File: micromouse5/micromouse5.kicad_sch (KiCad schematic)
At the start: 69 parts, among them J1 Conn_01x06_Pin, J2 Conn_01x06_Pin, J3 JST 2, J4 JST 1, J5 Conn_01x04_Pin, Q1 IR Receiver, Q2 IR Receiver, Q3 IR Receiver, Q4 IR Receiver, SW1 Button, SW2 EG1218, U1 HBridge, U2 Voltage Regulator, U3 MOSFET, U4 MOSFET, U5 MOSFET, U6 MOSFET, U7 STM32F205RGTx

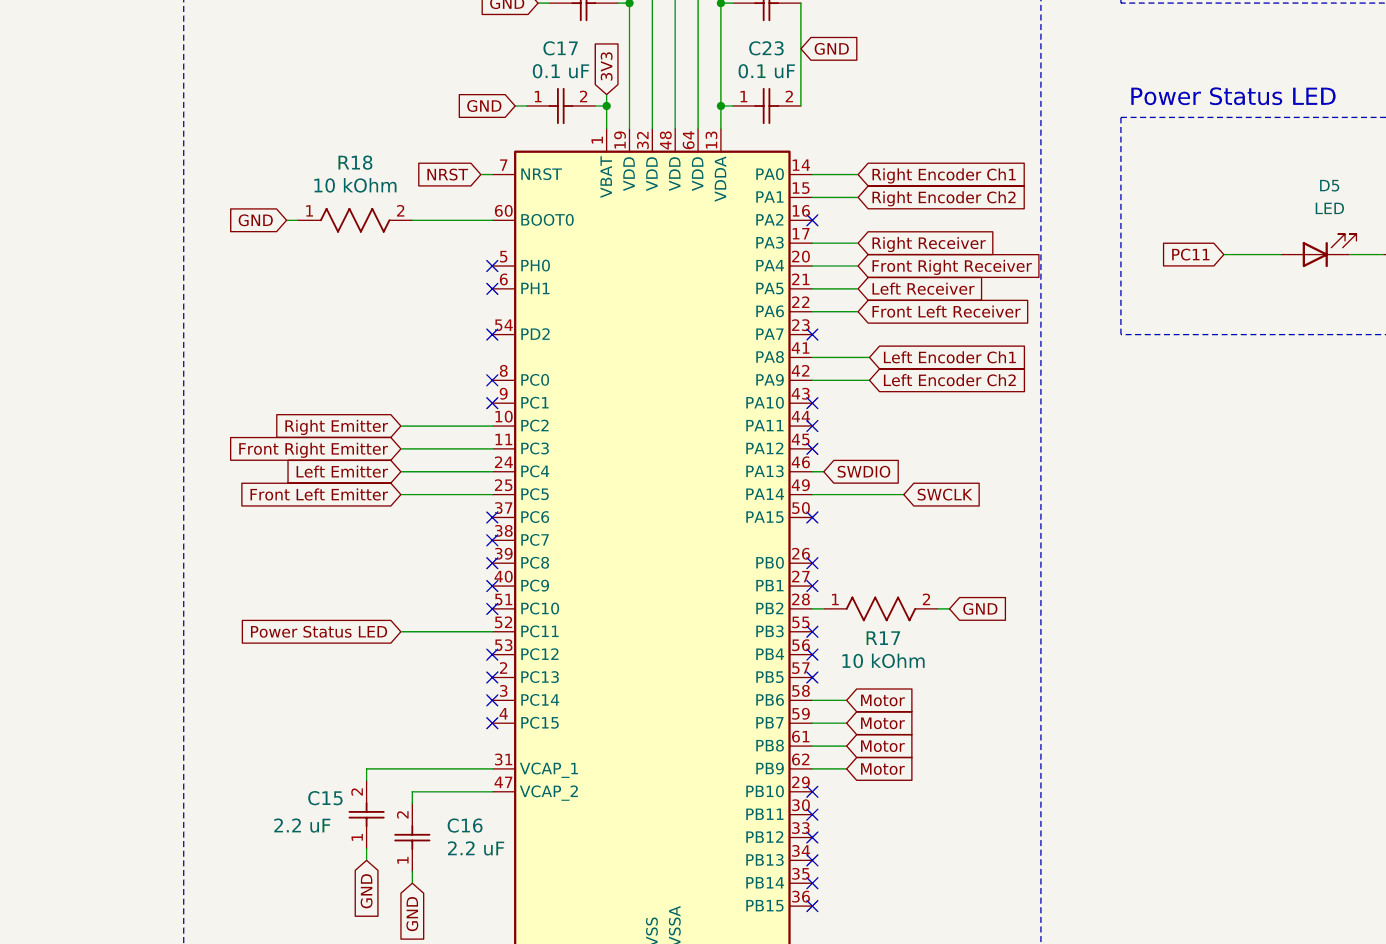
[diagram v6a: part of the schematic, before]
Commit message: Fixed pin association errors and mapped microcontroller pins to actual pins on our components.
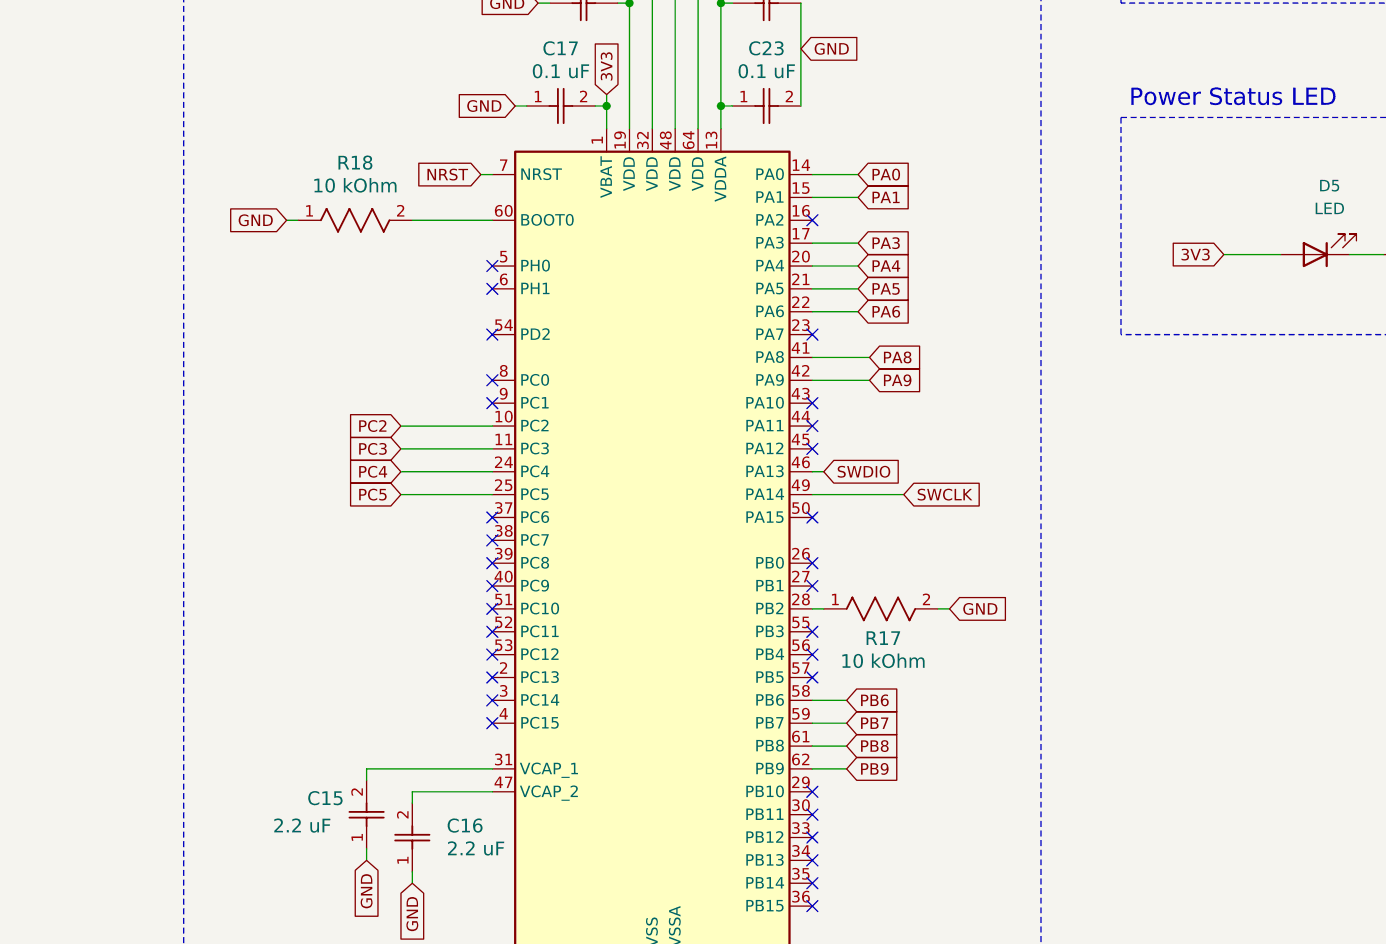
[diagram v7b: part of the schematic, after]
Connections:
- net Front Left Emitter is gone; now on net PC5: U7.25 (PC5)
- net Front Left Receiver is gone; now on net PA6: U7.22 (PA6)
- net Front Right Emitter is gone; now on net PC3: U7.11 (PC3)
- net Front Right Receiver is gone; now on net PA4: U7.20 (PA4)
- net Left Emitter is gone; now on net PC4: U7.24 (PC4)
- net Left Encoder Ch1 is gone; now on net PA8: U7.41 (PA8)
- net Left Encoder Ch2 is gone; now on net PA9: U7.42 (PA9)
- net Left Receiver is gone; now on net PA5: U7.21 (PA5)
- net PC11 is gone; now on net 3V3: D5.2 (A)
- net Right Emitter is gone; now on net PC2: U7.10 (PC2)
- net Right Encoder Ch1 is gone; now on net PA0: U7.14 (PA0)
- net Right Encoder Ch2 is gone; now on net PA1: U7.15 (PA1)
- net Right Receiver is gone; now on net PA3: U7.17 (PA3)
- net PB6: now also U7.58 (PB6)
- net PB7: now also U7.59 (PB7)
- net PB8: now also U7.61 (PB8)
- net PB9: now also U7.62 (PB9)
- removed net Motor: U7.58 (PB6), U7.59 (PB7), U7.61 (PB8), U7.62 (PB9)
- net Power Status LED: no longer names the net of U7.52 (PC11)
- no-connect marks 31 -> 32
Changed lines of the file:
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@@
 	)
 	(no_connect
+		(at 83.82 330.2)
+	)
+	(no_connect
 		(at 119.38 309.88)
 	)
@@
 	(wire
 		(pts
-			(xy 73.66 330.2) (xy 83.82 330.2)
-		)
-		(stroke
-			(width 0)
-			(type default)
-		)
-	)
-	(wire
-		(pts
 			(xy 121.92 143.51) (xy 121.92 148.59)
 		)
@@
 		)
 	)
-	(global_label "Right Encoder Ch1"
+	(global_label "PA0"
 		(shape input)
 		(at 124.46 279.4 0)
@@
 		)
 		(property "Intersheetrefs" "${INTERSHEET_REFS}"
-			(at 145.4668 279.4 0)
+			(at 131.0133 279.4 0)
 			(effects
 				(font
@@
 		)
 	)
-	(global_label "Motor"
+	(global_label "PB6"
 		(shape input)
 		(at 123.19 337.82 0)
@@
 		)
 		(property "Intersheetrefs" "${INTERSHEET_REFS}"
-			(at 131.4365 337.82 0)
+			(at 129.9247 337.82 0)
 			(effects
 				(font
@@
 		)
 	)
-	(global_label "Front Right Emitter"
+	(global_label "PC3"
 		(shape input)
 		(at 73.66 309.88 180)
@@
 		)
 		(property "Intersheetrefs" "${INTERSHEET_REFS}"
-			(at 52.1693 309.88 0)
+			(at 66.9253 309.88 0)
 			(effects
 				(font
@@
 		)
 	)
-	(global_label "Right Emitter"
+	(global_label "PC2"
 		(shape input)
 		(at 73.66 307.34 180)
@@
 		)
 		(property "Intersheetrefs" "${INTERSHEET_REFS}"
-			(at 58.0354 307.34 0)
+			(at 66.9253 307.34 0)
 			(effects
 				(font
@@
 		)
 	)
-	(global_label "Motor"
+	(global_label "PB7"
 		(shape input)
 		(at 123.19 340.36 0)
@@
 		)
 		(property "Intersheetrefs" "${INTERSHEET_REFS}"
-			(at 131.4365 340.36 0)
+			(at 129.9247 340.36 0)
 			(effects
 				(font
@@
 		)
 	)
-	(global_label "Front Right Receiver"
+	(global_label "PA4"
 		(shape input)
 		(at 124.46 289.56 0)
@@
 		)
 		(property "Intersheetrefs" "${INTERSHEET_REFS}"
-			(at 147.1604 289.56 0)
+			(at 131.0133 289.56 0)
 			(effects
 				(font
@@
 		)
 	)
-	(global_label "Right Receiver"
+	(global_label "PA3"
 		(shape input)
 		(at 124.46 287.02 0)
@@
 		)
 		(property "Intersheetrefs" "${INTERSHEET_REFS}"
-			(at 141.2943 287.02 0)
+			(at 131.0133 287.02 0)
 			(effects
 				(font
@@
 		)
 	)
-	(global_label "Right Encoder Ch2"
+	(global_label "PA1"
 		(shape input)
 		(at 124.46 281.94 0)
@@
 		)
 		(property "Intersheetrefs" "${INTERSHEET_REFS}"
-			(at 145.4668 281.94 0)
+			(at 131.0133 281.94 0)
 			(effects
 				(font
@@
 		)
 	)
-	(global_label "Front Left Emitter"
+	(global_label "PC5"
 		(shape input)
 		(at 73.66 314.96 180)
@@
 		)
 		(property "Intersheetrefs" "${INTERSHEET_REFS}"
-			(at 53.4997 314.96 0)
+			(at 66.9253 314.96 0)
 			(effects
 				(font
@@
 		)
 	)
-	(global_label "Left Receiver"
+	(global_label "PA5"
 		(shape input)
 		(at 124.46 292.1 0)
@@
 		)
 		(property "Intersheetrefs" "${INTERSHEET_REFS}"
-			(at 139.9639 292.1 0)
+			(at 131.0133 292.1 0)
 			(effects
 				(font
@@
 		)
 	)
-	(global_label "Left Encoder Ch1"
+	(global_label "PA8"
 		(shape input)
 		(at 125.73 299.72 0)
@@
 		)
 		(property "Intersheetrefs" "${INTERSHEET_REFS}"
-			(at 145.4064 299.72 0)
+			(at 132.2833 299.72 0)
 			(effects
 				(font
@@
 		)
 	)
-	(global_label "Motor"
+	(global_label "PB9"
 		(shape input)
 		(at 123.19 345.44 0)
@@
 		)
 		(property "Intersheetrefs" "${INTERSHEET_REFS}"
-			(at 131.4365 345.44 0)
+			(at 129.9247 345.44 0)
 			(effects
 				(font
@@
 		)
 	)
-	(global_label "Left Emitter"
+	(global_label "PC4"
 		(shape input)
 		(at 73.66 312.42 180)
@@
 		)
 		(property "Intersheetrefs" "${INTERSHEET_REFS}"
-			(at 59.3658 312.42 0)
+			(at 66.9253 312.42 0)
 			(effects
 				(font
@@
 		)
 	)
-	(global_label "Front Left Receiver"
+	(global_label "PA6"
 		(shape input)
 		(at 124.46 294.64 0)
@@
 		)
 		(property "Intersheetrefs" "${INTERSHEET_REFS}"
-			(at 145.83 294.64 0)
+			(at 131.0133 294.64 0)
 			(effects
 				(font
@@
 		)
 	)
-	(global_label "Motor"
+	(global_label "PB8"
 		(shape input)
 		(at 123.19 342.9 0)
@@
 		)
 		(property "Intersheetrefs" "${INTERSHEET_REFS}"
-			(at 131.4365 342.9 0)
+			(at 129.9247 342.9 0)
 			(effects
 				(font
@@
 		)
 	)
-	(global_label "Left Encoder Ch2"
+	(global_label "PA9"
 		(shape input)
 		(at 125.73 302.26 0)
@@
 		)
 		(property "Intersheetrefs" "${INTERSHEET_REFS}"
-			(at 145.4064 302.26 0)
+			(at 132.2833 302.26 0)
 			(effects
 				(font
@@
 		)
 	)
-	(global_label "PC11"
+	(global_label "3V3"
 		(shape input)
 		(at 165.1 288.29 180)
@@
 		)
 		(property "Intersheetrefs" "${INTERSHEET_REFS}"
-			(at 157.1558 288.29 0)
+			(at 158.6072 288.29 0)
 			(effects
 				(font
@@
 				(hide yes)
 			)
-		)
-	)
-	(global_label "Power Status LED"
-		(shape input)
-		(at 73.66 330.2 180)
-		(fields_autoplaced yes)
-		(effects
-			(font
-				(size 1.27 1.27)
-			)
-			(justify right)
-		)
-		(property "Intersheetrefs" "${INTERSHEET_REFS}"
-			(at 53.6812 330.2 0)
-			(effects
-				(font
-					(size 1.27 1.27)
-				)
-				(justify right)
-				(hide yes)
-			)

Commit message: Finished Schematic
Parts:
- D5: footprint (none) -> LED- Green:LED_LTST-C170GKT_LTO
- J1, J2: footprint (none) -> Connector_PinHeader_2.54mm:PinHeader_1x06_P2.54mm_Vertical
- J5: footprint (none) -> Connector_PinHeader_2.54mm:PinHeader_1x04_P2.54mm_Vertical
- R19: footprint RK73H2ARTTD4702F:RESC2012X60N -> micromouse5:RESC2012X60N (47kΩ)
- R21: footprint RK73H2ATTD3000F:RESC2012X60N -> Resistor- 300ohm:RESC2012X60N
- SW1: footprint Button_FP_FSM4JSMA:TE_FSM4JSMA -> Button:SW4_FSM4JSMA_TEC
- SW2: footprint SW_1218_EWI -> Switch:SW_1218_EWI
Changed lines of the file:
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@@
 			)
 		)
-		(property "Footprint" "RK73H2ARTTD4702F:RESC2012X60N"
+		(property "Footprint" "micromouse5:RESC2012X60N (47kΩ)"
 			(at 172.72 246.38 0)
 			(effects
@@
 			)
 		)
-		(property "Footprint" ""
+		(property "Footprint" "LED- Green:LED_LTST-C170GKT_LTO"
 			(at 175.26 288.29 0)
 			(effects
@@
 			)
 		)
-		(property "Footprint" "Button_FP_FSM4JSMA:TE_FSM4JSMA"
+		(property "Footprint" "Button:SW4_FSM4JSMA_TEC"
 			(at 196.85 243.84 0)
 			(effects
@@
 			)
 		)
-		(property "Footprint" ""
+		(property "Footprint" "Connector_PinHeader_2.54mm:PinHeader_1x06_P2.54mm_Vertical"
 			(at 35.56 78.74 0)
 			(effects
@@
 			)
 		)
-		(property "Footprint" ""
+		(property "Footprint" "Connector_PinHeader_2.54mm:PinHeader_1x06_P2.54mm_Vertical"
 			(at 78.74 78.74 0)
 			(effects
@@
 			)
 		)
-		(property "Footprint" ""
+		(property "Footprint" "Connector_PinHeader_2.54mm:PinHeader_1x04_P2.54mm_Vertical"
 			(at 54.61 190.5 0)
 			(effects
@@
 			)
 		)
-		(property "Footprint" "SW_1218_EWI"
+		(property "Footprint" "Switch:SW_1218_EWI"
 			(at 77.47 121.92 0)
 			(effects
@@
 			)
 		)
-		(property "Footprint" "RK73H2ATTD3000F:RESC2012X60N"
+		(property "Footprint" "Resistor- 300ohm:RESC2012X60N"
 			(at 193.04 288.29 0)
 			(effects
